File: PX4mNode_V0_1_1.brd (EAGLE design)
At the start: 48.6 x 34.9 mm, 133 parts, among them J201 DF13C-6P-1.25V, J202 DF13C-6P-1.25V, J203 DF13C-6P-1.25V, J301 DF13C-4P-1.25V, J401 DF13C-7P-1.25V, J402 DF13-4P-1.25V, J403 DF13C-4P-1.25V, J404 DF13C-4P-1.25V, J405 DF13C-4P-1.25V, J801 DF13C-3P-1.25V, M3_MOUNT1101 MOUNT-HOLE3.1MM, M3_MOUNT1102 MOUNT-HOLE3.1MM, M3_MOUNT1103 MOUNT-HOLE3.1MM, M3_MOUNT1104 MOUNT-HOLE3.1MM, U101 STM32F4X7VX, U401 MAX3051, U402 MAX3051, X101 3.2x2.5 mm / 24 MHz / 15 ppm

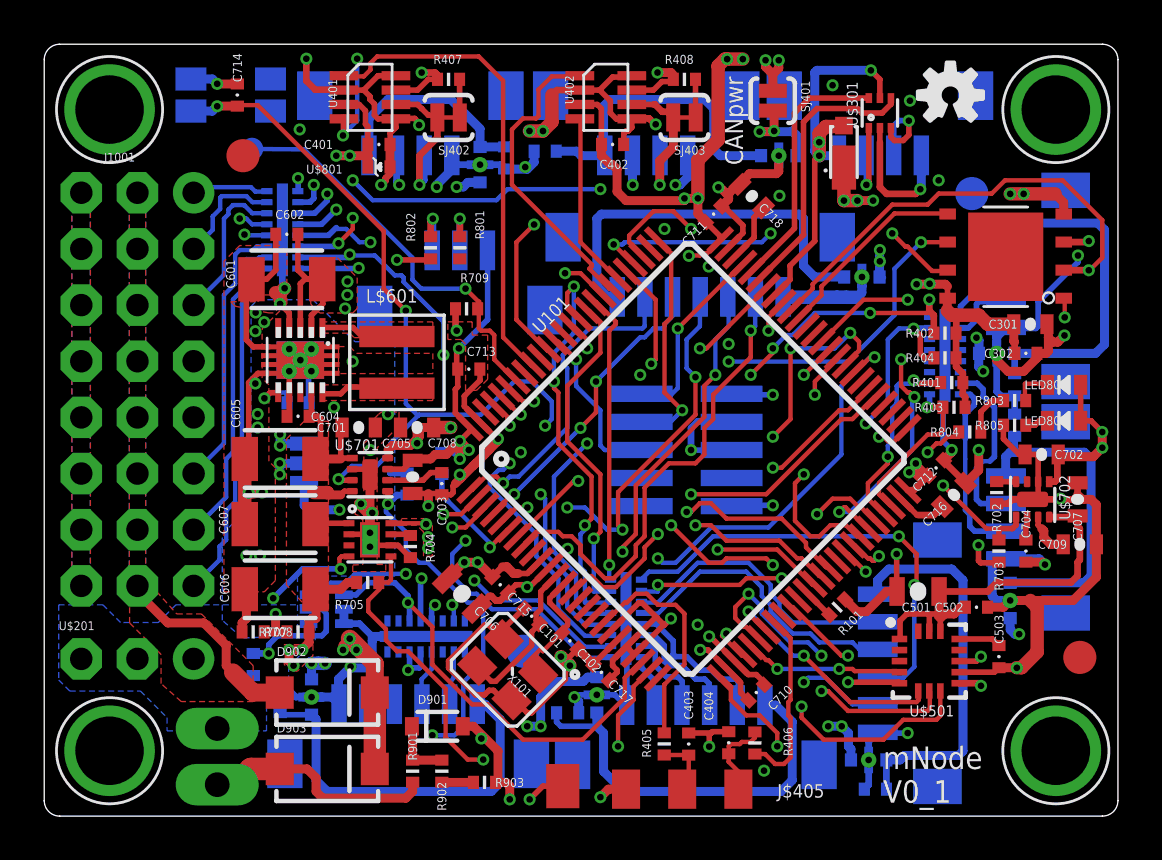
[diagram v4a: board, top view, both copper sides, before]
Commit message: SBUS output fitted
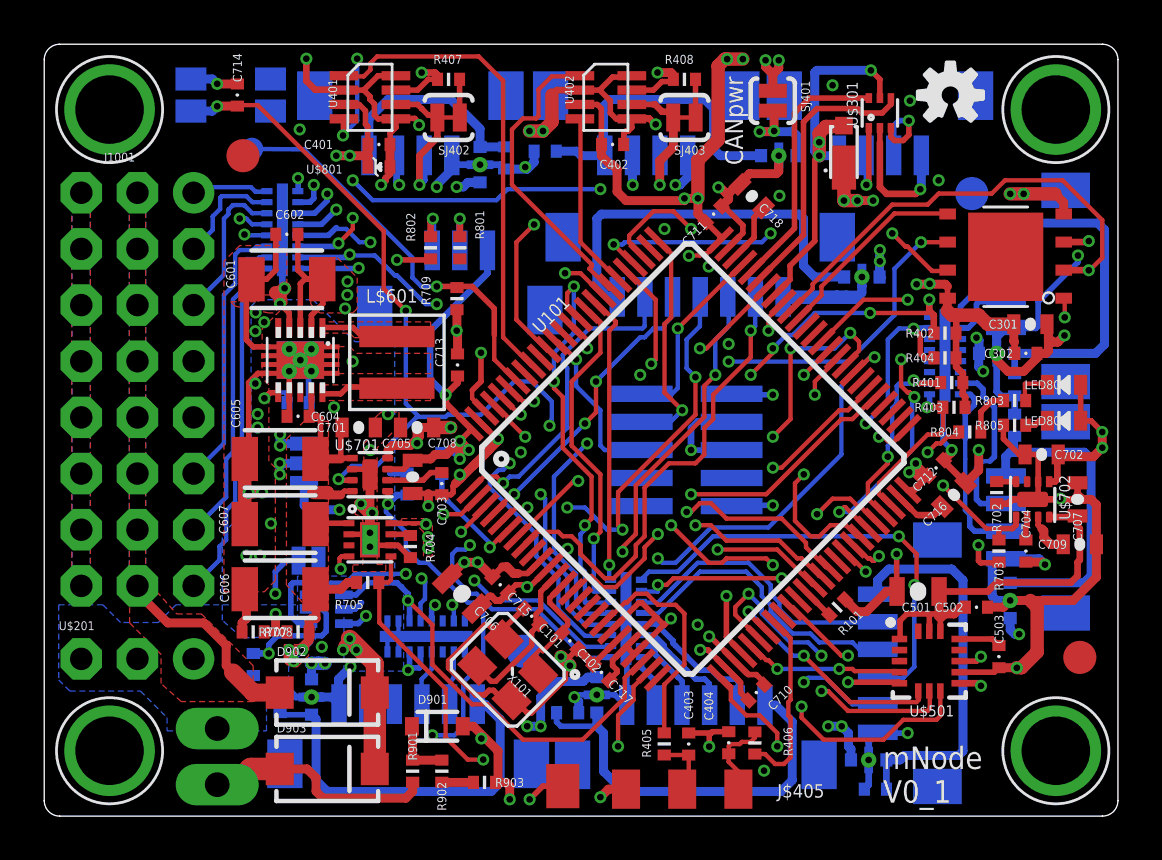
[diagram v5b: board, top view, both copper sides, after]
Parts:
- added JP4: (no value), SparkFun-Passives:SJ_2S-NO
- moved R709 0.63 mm to (27.9, 26.1), turned to 90 degrees
- moved C713 0.54 mm to (27.9, 23.1), turned to 90 degrees
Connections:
- new net N$5: JP4.1, U$1.4
- net FMU-CH8: now also JP4.2
- net FMU-UART8_TX: now also U$1.3
- net GND: now also L201.P$1, L201.P$15, L201.P$16, L201.P$2; no longer U$1.3
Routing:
- net FMU-UART8_TX: track 0.00 -> 25.7 mm, vias 0 -> 2
- net FMU-CH8: track 26.5 -> 47.8 mm, vias 2 -> 3
- net !VDD_5V_PERIPH_OC: track 39.7 -> 33.3 mm, vias 3 -> 2
- net GND: track 231.7 -> 226.8 mm, vias 59 -> 60
- net N$5: track 0.00 -> 4.49 mm
- net VDD_5V_SENS: track 25.5 -> 29.8 mm
- net FMU-UART8_RX: track 16.4 -> 18.0 mm
- net VDD_5V_PERIPH: track 66.6 -> 68.0 mm
- net !SPI_EXT_NSS: track 23.6 -> 22.8 mm
- net !VDD_5V_PERIPH_EN: track 47.6 -> 46.9 mm
- net FMU-VDD_3V3: track 130.1 -> 130.4 mm, vias 22 -> 23

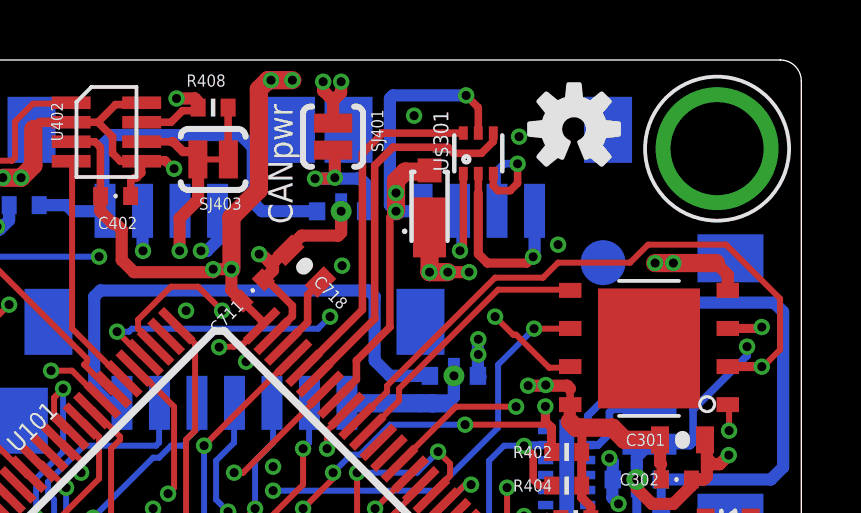
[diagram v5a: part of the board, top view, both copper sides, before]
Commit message: Shuffled USB ESD protector to make a little more space
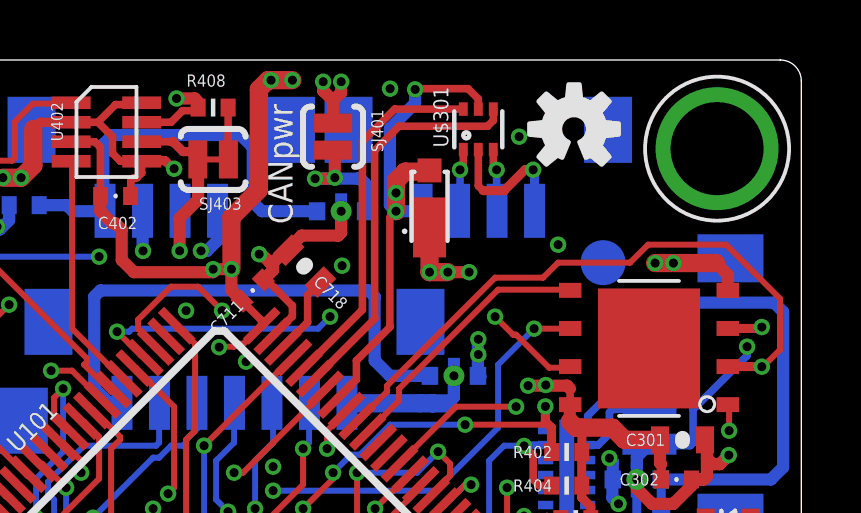
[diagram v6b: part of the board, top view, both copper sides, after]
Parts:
- moved U$301 0.80 mm to (47.0, 35.3)
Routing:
- net OTG_DM1: track 4.18 -> 2.11 mm
- net OTG_DP1: track 4.09 -> 2.25 mm
- net GND: track 226.8 -> 225.3 mm
- net VBUS: track 18.7 -> 18.0 mm
- net OTG_FS_DP: track 11.6 -> 12.2 mm
- net OTG_FS_DM: track 12.7 -> 13.2 mm

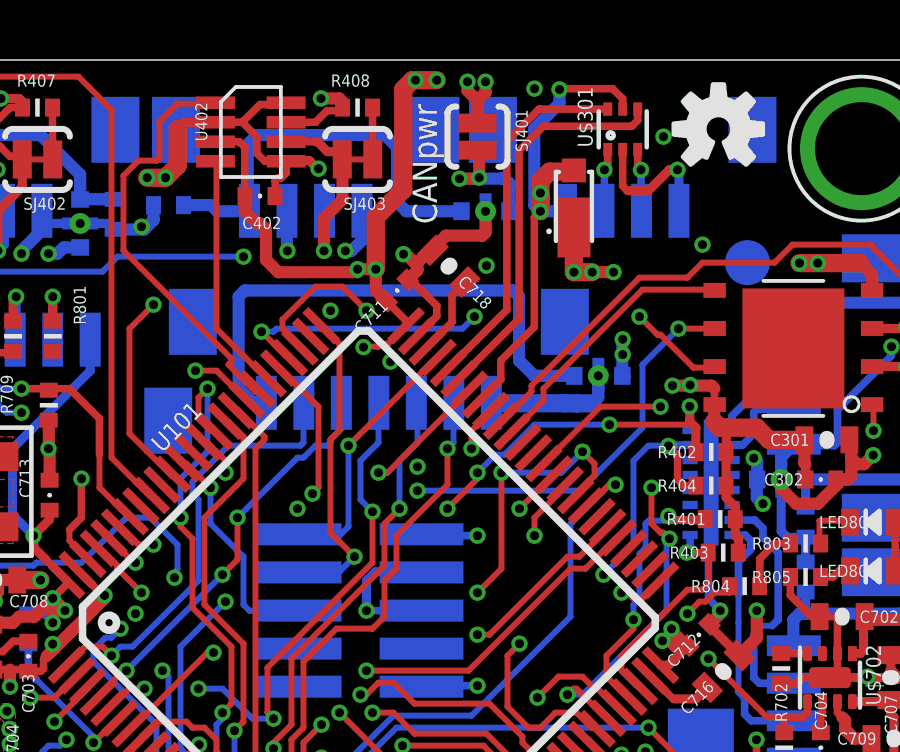
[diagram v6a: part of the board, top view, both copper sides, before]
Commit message: Another autorouter detangle tidyup
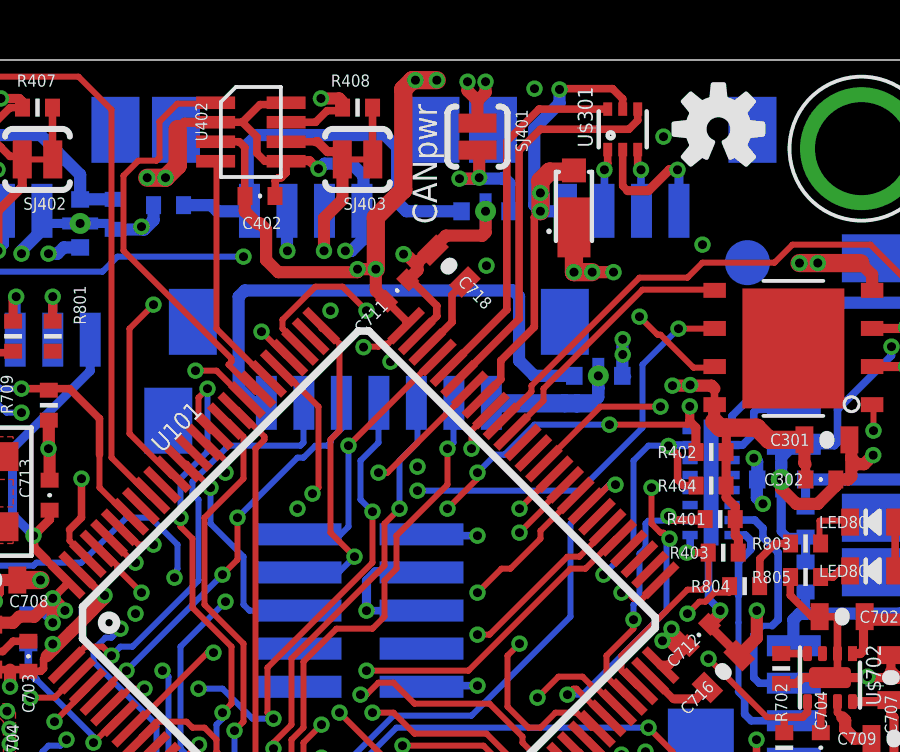
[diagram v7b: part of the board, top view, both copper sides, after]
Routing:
- net FMU-USART3_RTS: track 37.7 -> 33.3 mm, vias 5 -> 3
- net GND: track 225.3 -> 228.5 mm
- net SDIO_D3: vias 3 -> 2
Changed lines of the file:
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@@
 <layer number="1" name="Top" color="4" fill="1" visible="yes" active="yes"/>
 <layer number="2" name="Ground" color="2" fill="10" visible="no" active="yes"/>
-<layer number="3" name="Horizontal" color="13" fill="15" visible="no" active="yes"/>
+<layer number="3" name="Horizontal" color="13" fill="15" visible="yes" active="yes"/>
 <layer number="4" name="Route4" color="1" fill="4" visible="no" active="no"/>
 <layer number="5" name="Route5" color="4" fill="4" visible="no" active="no"/>
@@
 <layer number="12" name="Route12" color="1" fill="5" visible="no" active="no"/>
 <layer number="13" name="Route13" color="4" fill="5" visible="no" active="no"/>
-<layer number="14" name="Vertical" color="14" fill="15" visible="no" active="yes"/>
+<layer number="14" name="Vertical" color="14" fill="15" visible="yes" active="yes"/>
 <layer number="15" name="Power" color="11" fill="15" visible="no" active="yes"/>
 <layer number="16" name="Bottom" color="1" fill="1" visible="yes" active="yes"/>
 <layer number="17" name="Pads" color="2" fill="1" visible="yes" active="yes"/>
 <layer number="18" name="Vias" color="2" fill="1" visible="yes" active="yes"/>
-<layer number="19" name="Unrouted" color="14" fill="1" visible="no" active="yes"/>
+<layer number="19" name="Unrouted" color="14" fill="1" visible="yes" active="yes"/>
 <layer number="20" name="Dimension" color="15" fill="1" visible="yes" active="yes"/>
 <layer number="21" name="tPlace" color="7" fill="1" visible="yes" active="yes"/>
@@
 <contactref element="U101" pad="70"/>
 <contactref element="U$301" pad="4"/>
-<wire x1="47.3472" y1="35.4472" x2="44.396" y2="35.4472" width="0.254" layer="1"/>
-<wire x1="44.396" y1="35.4472" x2="43.5864" y2="34.6376" width="0.254" layer="1"/>
+<wire x1="47.2472" y1="35.3472" x2="44.296" y2="35.3472" width="0.254" layer="1"/>
+<wire x1="44.296" y1="35.3472" x2="43.5864" y2="34.6376" width="0.254" layer="1"/>
 <wire x1="43.5864" y1="34.6376" x2="43.5864" y2="29.028946875" width="0.254" layer="1"/>
 <wire x1="43.5864" y1="29.028946875" x2="41.586778125" y2="27.029325" width="0.254" layer="1"/>
-<wire x1="47.3472" y1="35.4472" x2="47.5408" y2="35.6408" width="0.254" layer="1"/>
+<wire x1="47.2472" y1="35.3472" x2="47.5408" y2="35.6408" width="0.254" layer="1"/>
 <wire x1="47.5408" y1="35.6408" x2="47.5408" y2="36.019" width="0.254" layer="1"/>
 </signal>
@@
 <wire x1="35.8" y1="27.8" x2="35.9" y2="27.8" width="0.2" layer="1"/>
 <wire x1="35" y1="28.6" x2="35.8" y2="27.8" width="0.2" layer="1"/>
-<wire x1="41.7" y1="28.7" x2="35.5" y2="28.7" width="0.2" layer="16"/>
-<wire x1="35.5" y1="28.7" x2="35.4" y2="28.6" width="0.2" layer="16"/>
-<wire x1="35.4" y1="28.6" x2="35" y2="28.6" width="0.2" layer="16"/>
-<wire x1="42.1" y1="29.1" x2="41.7" y2="28.7" width="0.2" layer="16"/>
 <wire x1="47.6" y1="29.1" x2="42.1" y2="29.1" width="0.2" layer="3"/>
 <wire x1="48.2" y1="28.5" x2="47.6" y2="29.1" width="0.2" layer="1"/>
@@
 <wire x1="50" y1="27.4" x2="50.1054" y2="27.4366" width="0.2" layer="1"/>
 <via x="35" y="28.6" extent="1-16" drill="0.3" diameter="0.55"/>
-<via x="42.1" y="29.1" extent="1-16" drill="0.3" diameter="0.55"/>
 <via x="47.6" y="29.1" extent="1-16" drill="0.3" diameter="0.55"/>
+<wire x1="42.1" y1="29.1" x2="39.3" y2="29.1" width="0.254" layer="3"/>
+<wire x1="39.3" y1="29.1" x2="38.9" y2="28.7" width="0.254" layer="3"/>
+<wire x1="38.9" y1="28.7" x2="38" y2="28.7" width="0.254" layer="3"/>
+<wire x1="38" y1="28.7" x2="37.9" y2="28.6" width="0.254" layer="3"/>
+<wire x1="37.9" y1="28.6" x2="35" y2="28.6" width="0.254" layer="3"/>
 </signal>
 <signal name="!GYRO_CS">
@@
 <contactref element="U101" pad="59"/>
 <contactref element="L202" pad="P$1"/>
-<wire x1="46.1" y1="23.8" x2="45.5" y2="23.2" width="0.2" layer="1"/>
-<wire x1="46.1" y1="24.2" x2="46.1" y2="23.8" width="0.2" layer="1"/>
-<wire x1="45.7" y1="24.6" x2="46.1" y2="24.2" width="0.2" layer="1"/>
-<wire x1="45" y1="23.9" x2="45.7" y2="24.6" width="0.2" layer="16"/>
-<wire x1="43" y1="23.9" x2="45" y2="23.9" width="0.2" layer="16"/>
-<wire x1="43" y1="20.7" x2="43" y2="23.9" width="0.2" layer="1"/>
 <wire x1="42.2" y1="19.9" x2="43" y2="20.7" width="0.2" layer="1"/>
 <wire x1="42" y1="20.1" x2="42.2" y2="19.9" width="0.2" layer="3"/>
@@
 <wire x1="45.5" y1="23.2" x2="45.475865625" y2="23.140240625" width="0.2" layer="1"/>
 <wire x1="34.8" y1="9.9" x2="34.86" y2="9.934" width="0.2" layer="16"/>
-<via x="45.7" y="24.6" extent="1-16" drill="0.3" diameter="0.55"/>
-<via x="43" y="23.9" extent="1-16" drill="0.3" diameter="0.55"/>
 <via x="42.2" y="19.9" extent="1-16" drill="0.3" diameter="0.55"/>
 <via x="30.8" y="19.2" extent="1-16" drill="0.3" diameter="0.55"/>
 <via x="28.5" y="15" extent="1-16" drill="0.3" diameter="0.55"/>
+<wire x1="43" y1="20.7" x2="43.3" y2="20.7" width="0.2" layer="1"/>
+<wire x1="43.3" y1="20.7" x2="44.3" y2="21.7" width="0.2" layer="1"/>
+<wire x1="44.3" y1="21.7" x2="44.3" y2="21.964375" width="0.2" layer="1"/>
+<wire x1="44.3" y1="21.964375" x2="45.475865625" y2="23.140240625" width="0.2" layer="1"/>
 </signal>
 <signal name="FMU-UART7_TX">
@@
 <wire x1="44.2" y1="23.5" x2="40.1" y2="27.6" width="0.2" layer="14"/>
 <wire x1="44.2" y1="22.5" x2="44.2" y2="23.5" width="0.2" layer="14"/>
-<wire x1="44.1" y1="22.4" x2="44.2" y2="22.5" width="0.2" layer="14"/>
-<wire x1="44.1" y1="21.8" x2="44.1" y2="22.4" width="0.2" layer="14"/>
-<wire x1="44.1" y1="22.4" x2="44.1" y2="21.8" width="0.2" layer="1"/>
-<wire x1="45.1" y1="23.4" x2="44.1" y2="22.4" width="0.2" layer="1"/>
+<wire x1="43.6" y1="21.9" x2="44.2" y2="22.5" width="0.2" layer="14"/>
 <wire x1="22.5" y1="29.3" x2="22.4536" y2="29.3624" width="0.2" layer="16"/>
 <wire x1="45.1" y1="23.4" x2="45.1223125" y2="23.49379375" width="0.2" layer="1"/>
 <via x="24" y="28.7" extent="1-16" drill="0.3" diameter="0.55"/>
 <via x="39.3" y="27.6" extent="1-16" drill="0.3" diameter="0.55"/>
-<via x="44.1" y="21.8" extent="1-16" drill="0.3" diameter="0.55"/>
+<via x="43.6" y="21.9" extent="1-16" drill="0.3" diameter="0.55"/>
+<wire x1="43.6" y1="21.9" x2="44.4" y2="22.7" width="0.2" layer="1"/>
+<wire x1="44.4" y1="22.7" x2="44.4" y2="22.77148125" width="0.2" layer="1"/>
+<wire x1="44.4" y1="22.77148125" x2="45.1223125" y2="23.49379375" width="0.2" layer="1"/>
 </signal>
 <signal name="FMU-CH8">
@@
 <contactref element="L201" pad="P$2"/>
 <via x="19.4976" y="15.9784" extent="1-16" drill="0.3" diameter="0.55"/>
-<wire x1="46.228" y1="27.5272" x2="46.228" y2="27.1272" width="0" layer="19" extent="16-16"/>
 <wire x1="48.9158" y1="32.628" x2="48.9158" y2="33.9482" width="0.3048" layer="16"/>
 <wire x1="48.9158" y1="33.9482" x2="48.868" y2="33.996" width="0.3048" layer="16"/>
@@
 <wire x1="47.2" y1="33.3" x2="47.0408" y2="33.4592" width="0.254" layer="1"/>
 <wire x1="47.0408" y1="33.4592" x2="47.0408" y2="34.669" width="0.254" layer="1"/>
+<wire x1="38.3" y1="32.8" x2="38.4" y2="32.9" width="0.4064" layer="16"/>
+<wire x1="38.4" y1="33.8" x2="38" y2="34.2" width="0.4064" layer="16"/>
+<wire x1="38" y1="34.2" x2="37.1" y2="34.2" width="0.4064" layer="16"/>
+<wire x1="37.1" y1="34.2" x2="36.9" y2="34" width="0.4064" layer="16"/>
+<wire x1="38.4" y1="33.8" x2="38.4" y2="32.7" width="0.4064" layer="16"/>
+<wire x1="38.4" y1="32.6786" x2="38.3494" y2="32.628" width="0.4064" layer="16"/>
+<wire x1="38.4" y1="32.6786" x2="38.4" y2="32.7" width="0.4064" layer="16"/>
+<wire x1="38.4" y1="32.7" x2="38.3" y2="32.8" width="0.4064" layer="16"/>
+<wire x1="46.228" y1="27.1272" x2="46.228" y2="27.5272" width="0" layer="19" extent="16-16"/>
 </signal>
 <signal name="N$4">
